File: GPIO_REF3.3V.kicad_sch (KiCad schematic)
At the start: 14 parts

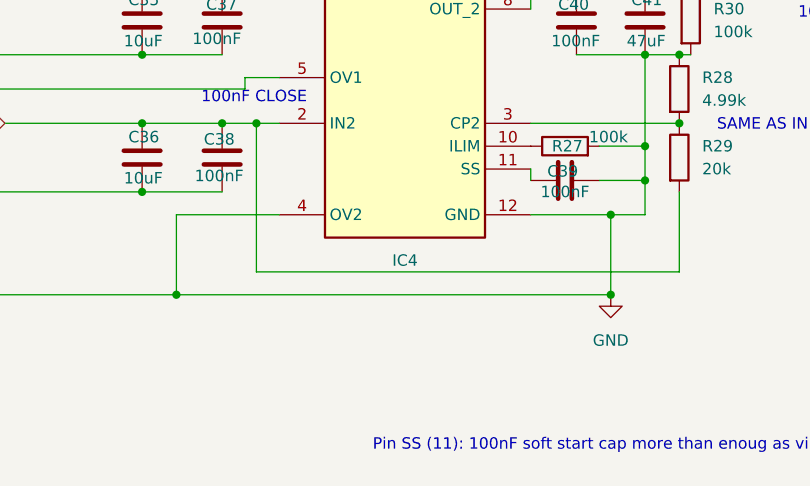
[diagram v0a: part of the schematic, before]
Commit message: added Gyroscope and Accelerometer part (4x) over IIC
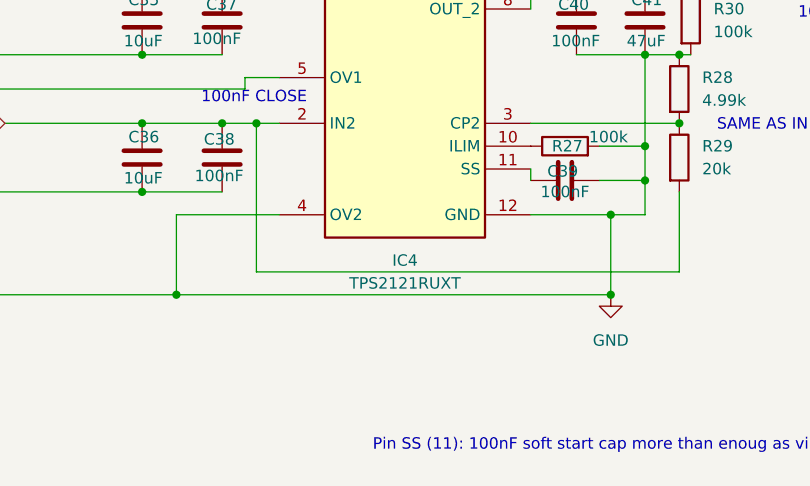
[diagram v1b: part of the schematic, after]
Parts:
- IC4: value ~ -> TPS2121RUXT
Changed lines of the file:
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@@
 			)
 		)
-		(property "Value" "~"
+		(property "Value" "TPS2121RUXT"
 			(at 146.05 121.92 0)
 			(effects

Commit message: multiple chainges on PCB
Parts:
- IC4: Order (none) -> Ordered=True
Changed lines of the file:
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@@
+			)
+		)
+		(property "Order" "Ordered=True"
+			(at 132.08 88.9 0)
+			(effects
+				(font
+					(size 1.27 1.27)
+				)
+				(hide yes)
 			)
 		)

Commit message: Power changes
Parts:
- renumbered IC4 to IC5, R14 to R25
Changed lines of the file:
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@@
 		)
 		(instances
-			(project ""
-				(path "/ce1819b2-f280-40ed-834f-6fe4d12f809d/c1998c4d-3f9a-4761-b447-a813532738a0/e46d3b44-477e-48ec-b385-9b4870813d66"
+			(project "nautilus_mainboard"
+				(path "/ce1819b2-f280-40ed-834f-6fe4d12f809d/c1998c4d-3f9a-4761-b447-a813532738a0/b9b676f4-45ad-4d4b-96a9-894c1f9d02cb"
 					(reference "C39")
 					(unit 1)
@@
 		(instances
 			(project "nautilus_mainboard"
-				(path "/ce1819b2-f280-40ed-834f-6fe4d12f809d/c1998c4d-3f9a-4761-b447-a813532738a0/e46d3b44-477e-48ec-b385-9b4870813d66"
+				(path "/ce1819b2-f280-40ed-834f-6fe4d12f809d/c1998c4d-3f9a-4761-b447-a813532738a0/b9b676f4-45ad-4d4b-96a9-894c1f9d02cb"
 					(reference "C40")
 					(unit 1)
@@
 		(instances
 			(project "nautilus_mainboard"
-				(path "/ce1819b2-f280-40ed-834f-6fe4d12f809d/c1998c4d-3f9a-4761-b447-a813532738a0/e46d3b44-477e-48ec-b385-9b4870813d66"
+				(path "/ce1819b2-f280-40ed-834f-6fe4d12f809d/c1998c4d-3f9a-4761-b447-a813532738a0/b9b676f4-45ad-4d4b-96a9-894c1f9d02cb"
 					(reference "R26")
 					(unit 1)
@@
 		(on_board yes)
 		(dnp no)
-		(property "Reference" "R14"
+		(property "Reference" "R25"
 			(at 129.54 87.122 90)
 			(effects
@@
 		(instances
 			(project "nautilus_mainboard"
-				(path "/ce1819b2-f280-40ed-834f-6fe4d12f809d/c1998c4d-3f9a-4761-b447-a813532738a0/e46d3b44-477e-48ec-b385-9b4870813d66"
-					(reference "R14")
+				(path "/ce1819b2-f280-40ed-834f-6fe4d12f809d/c1998c4d-3f9a-4761-b447-a813532738a0/b9b676f4-45ad-4d4b-96a9-894c1f9d02cb"
+					(reference "R25")
 					(unit 1)
 				)
@@
 		(instances
 			(project "nautilus_mainboard"
-				(path "/ce1819b2-f280-40ed-834f-6fe4d12f809d/c1998c4d-3f9a-4761-b447-a813532738a0/e46d3b44-477e-48ec-b385-9b4870813d66"
+				(path "/ce1819b2-f280-40ed-834f-6fe4d12f809d/c1998c4d-3f9a-4761-b447-a813532738a0/b9b676f4-45ad-4d4b-96a9-894c1f9d02cb"
 					(reference "R28")
 					(unit 1)
@@
 		(instances
 			(project "nautilus_mainboard"
-				(path "/ce1819b2-f280-40ed-834f-6fe4d12f809d/c1998c4d-3f9a-4761-b447-a813532738a0/e46d3b44-477e-48ec-b385-9b4870813d66"
+				(path "/ce1819b2-f280-40ed-834f-6fe4d12f809d/c1998c4d-3f9a-4761-b447-a813532738a0/b9b676f4-45ad-4d4b-96a9-894c1f9d02cb"
 					(reference "C37")
 					(unit 1)
@@
 		(dnp no)
 		(fields_autoplaced yes)
-		(property "Reference" "#PWR033"
+		(property "Reference" "#PWR030"
 			(at 168.91 129.54 0)
 			(effects
@@
 		(instances
 			(project "nautilus_mainboard"
-				(path "/ce1819b2-f280-40ed-834f-6fe4d12f809d/c1998c4d-3f9a-4761-b447-a813532738a0/e46d3b44-477e-48ec-b385-9b4870813d66"
-					(reference "#PWR033")
+				(path "/ce1819b2-f280-40ed-834f-6fe4d12f809d/c1998c4d-3f9a-4761-b447-a813532738a0/b9b676f4-45ad-4d4b-96a9-894c1f9d02cb"
+					(reference "#PWR030")
 					(unit 1)
 				)
@@
 		(instances
 			(project "nautilus_mainboard"
-				(path "/ce1819b2-f280-40ed-834f-6fe4d12f809d/c1998c4d-3f9a-4761-b447-a813532738a0/e46d3b44-477e-48ec-b385-9b4870813d66"
+				(path "/ce1819b2-f280-40ed-834f-6fe4d12f809d/c1998c4d-3f9a-4761-b447-a813532738a0/b9b676f4-45ad-4d4b-96a9-894c1f9d02cb"
 					(reference "C41")
 					(unit 1)
@@
 		(instances
 			(project "nautilus_mainboard"
-				(path "/ce1819b2-f280-40ed-834f-6fe4d12f809d/c1998c4d-3f9a-4761-b447-a813532738a0/e46d3b44-477e-48ec-b385-9b4870813d66"
+				(path "/ce1819b2-f280-40ed-834f-6fe4d12f809d/c1998c4d-3f9a-4761-b447-a813532738a0/b9b676f4-45ad-4d4b-96a9-894c1f9d02cb"
 					(reference "C35")
 					(unit 1)
@@
 		(instances
 			(project "nautilus_mainboard"
-				(path "/ce1819b2-f280-40ed-834f-6fe4d12f809d/c1998c4d-3f9a-4761-b447-a813532738a0/e46d3b44-477e-48ec-b385-9b4870813d66"
+				(path "/ce1819b2-f280-40ed-834f-6fe4d12f809d/c1998c4d-3f9a-4761-b447-a813532738a0/b9b676f4-45ad-4d4b-96a9-894c1f9d02cb"
 					(reference "R29")
 					(unit 1)
@@
 		)
 		(instances
-			(project ""
-				(path "/ce1819b2-f280-40ed-834f-6fe4d12f809d/c1998c4d-3f9a-4761-b447-a813532738a0/e46d3b44-477e-48ec-b385-9b4870813d66"
+			(project "nautilus_mainboard"
+				(path "/ce1819b2-f280-40ed-834f-6fe4d12f809d/c1998c4d-3f9a-4761-b447-a813532738a0/b9b676f4-45ad-4d4b-96a9-894c1f9d02cb"
 					(reference "R30")
 					(unit 1)
@@
 		(instances
 			(project "nautilus_mainboard"
-				(path "/ce1819b2-f280-40ed-834f-6fe4d12f809d/c1998c4d-3f9a-4761-b447-a813532738a0/e46d3b44-477e-48ec-b385-9b4870813d66"
+				(path "/ce1819b2-f280-40ed-834f-6fe4d12f809d/c1998c4d-3f9a-4761-b447-a813532738a0/b9b676f4-45ad-4d4b-96a9-894c1f9d02cb"
 					(reference "C38")
 					(unit 1)
@@
 		(instances
 			(project "nautilus_mainboard"
-				(path "/ce1819b2-f280-40ed-834f-6fe4d12f809d/c1998c4d-3f9a-4761-b447-a813532738a0/e46d3b44-477e-48ec-b385-9b4870813d66"
+				(path "/ce1819b2-f280-40ed-834f-6fe4d12f809d/c1998c4d-3f9a-4761-b447-a813532738a0/b9b676f4-45ad-4d4b-96a9-894c1f9d02cb"
 					(reference "R27")
 					(unit 1)
@@
 		(dnp no)
 		(fields_autoplaced yes)
-		(property "Reference" "IC4"
+		(property "Reference" "IC5"
 			(at 146.05 119.38 0)
 			(effects
@@
 		(instances
 			(project "nautilus_mainboard"
-				(path "/ce1819b2-f280-40ed-834f-6fe4d12f809d/c1998c4d-3f9a-4761-b447-a813532738a0/e46d3b44-477e-48ec-b385-9b4870813d66"
-					(reference "IC4")
+				(path "/ce1819b2-f280-40ed-834f-6fe4d12f809d/c1998c4d-3f9a-4761-b447-a813532738a0/b9b676f4-45ad-4d4b-96a9-894c1f9d02cb"
+					(reference "IC5")
 					(unit 1)
 				)
@@
 		(instances
 			(project "nautilus_mainboard"
-				(path "/ce1819b2-f280-40ed-834f-6fe4d12f809d/c1998c4d-3f9a-4761-b447-a813532738a0/e46d3b44-477e-48ec-b385-9b4870813d66"
+				(path "/ce1819b2-f280-40ed-834f-6fe4d12f809d/c1998c4d-3f9a-4761-b447-a813532738a0/b9b676f4-45ad-4d4b-96a9-894c1f9d02cb"
 					(reference "C36")
 					(unit 1)

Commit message: chore: more cleanup
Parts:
- removed C35, C36: 10uF, Capacitor_SMD:C_1210_3225Metric, symbol #dzdb:s_cap/C-MUR-GRM32EC72A106KE05
- removed C37, C38, C40: 100nF, Capacitor_SMD:C_0603_1608Metric, symbol #dzdb:g_cap/C-100n-0603
- removed C41: 47uF, Capacitor_SMD:C_0805_2012Metric, symbol #dzdb:s_cap/C-MUR-GRM21BR61A476ME15
- removed IC5: TPS2121RUXT, dz_dio:TI_Switchover_TPS2121RUXT, symbol #dzdb:s_misc/TEXA-595-TPS2121RUXT
- removed R25: 15.4k, Resistor_SMD:R_0603_1608Metric, symbol #dzdb:g_res/R-15.4k-0603
- removed R26, R28: 4.99k, Resistor_SMD:R_0603_1608Metric, symbol #dzdb:g_res/R-4.99k-0603
- removed R29: 20k, Resistor_SMD:R_0603_1608Metric, symbol #dzdb:g_res/R-20k-0603
- removed R30: 100k, Resistor_SMD:R_0603_1608Metric, symbol #dzdb:g_res/R-100k-0603
- added C48, C49: 10uF, Capacitor_SMD:C_1210_3225Metric, symbol #dzdb:s_cap/C-MUR-GRM32EC72A106KE05
- added C50, C51, C52: 100nF, Capacitor_SMD:C_0603_1608Metric, symbol #dzdb:g_cap/C-100n-0603
- added C54: 47uF, Capacitor_SMD:C_0805_2012Metric, symbol #dzdb:s_cap/C-MUR-GRM21BR61A476ME15
- added IC3: TPS2121RUXT, dz_dio:TI_Switchover_TPS2121RUXT, symbol #dzdb:s_misc/TEXA-595-TPS2121RUXT
- added R14: 100k, Resistor_SMD:R_0603_1608Metric, symbol #dzdb:g_res/R-100k-0603
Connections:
- net CM4_OUT_3.3V: now also C49.1, C51.1, IC3.2 (IN2)
- net GND: now also C39.1, R27.1, C48.2, C49.2, C50.2, C51.2, C52.2, C54.2, IC3.12 (GND), IC3.3 (CP2), IC3.4 (OV2), IC3.5 (OV1), R14.2; no longer C39.2, R27.2
- net GPIO_VREF_3.3V: now also C52.1, C54.1, IC3.1 (OUT_1), IC3.8 (OUT_2), R14.1
- net STM_IN_3.3V: now also C48.1, C50.1, IC3.6 (PR1), IC3.7 (IN1)
- new net: C39.2, IC3.11 (SS)
- new net: IC3.10 (ILIM), R27.2
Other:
- note removed: "100nF CLOSE"
- note removed: "SAME AS IN 5V"
- note removed: "V-div (same ratio as 5V)"
- company: (none) -> Davide
- moved on the sheet: C39, R27

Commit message: chore: Loads of redoing stuff. Added a Changelog
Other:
- title: (none) -> Nautilus_Mainboard
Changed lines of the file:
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@@
 	(paper "A4")
 	(title_block
+		(title "Nautilus_Mainboard")
 		(date "2025-11-19")
 		(rev "0")

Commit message: chore: routed many parts together. added testpoints
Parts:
- added TP13: Test Point, TestPoint:TestPoint_Pad_D1.5mm, symbol #dzdb:g_mech/M-TEST-SMT_1.5mm_round
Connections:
- net GPIO_VREF_3.3V: now also TP13.1
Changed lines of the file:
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@@
+		)
+	)
+	(symbol
+		(lib_id "#dzdb:g_mech/M-TEST-SMT_1.5mm_round")
+		(at 172.72 77.47 0)
+		(unit 1)
+		(exclude_from_sim no)
+		(in_bom yes)
+		(on_board yes)
+		(dnp no)
+		(property "Reference" "TP13"
+			(at 175.26 72.8979 0)
+			(effects
+				(font
+					(size 1.27 1.27)
+				)
+				(justify left)
+			)
+		)
+		(property "Value" "Test Point"
+			(at 175.26 74.93 0)
+			(effects
+				(font
+					(size 1.27 1.27)
+				)
+				(justify left)
+			)
+		)
+		(property "Footprint" "TestPoint:TestPoint_Pad_D1.5mm"
+			(at 177.8 77.47 0)
+			(effects
+				(font
+					(size 1.27 1.27)
+				)
+				(hide yes)
+			)
+		)
+		(property "Datasheet" "~"
+			(at 177.8 77.47 0)
+			(effects
+				(font
+					(size 1.27 1.27)
+				)
+				(hide yes)
+			)
+		)
+		(property "Description" "SMT Test Point 1.5mm round"
+			(at 172.72 77.47 0)
+			(effects
+				(font
+					(size 1.27 1.27)
+				)
+				(hide yes)
+			)
+		)
+		(property "IPN" "M-TEST-SMT_1.5mm_round"
+			(at 172.72 77.47 0)
+			(effects
+				(font
+					(size 1.27 1.27)
+				)
+				(hide yes)
+			)
+		)
+		(property "Comments" "TestPoint 1.5mm"
+			(at 172.72 77.47 0)
+			(effects
+				(font
+					(size 1.27 1.27)
+				)
+				(hide yes)
+			)
+		)
+		(pin "1"
+		)
+		(instances
+			(project "nautilus_mainboard"
+				(path "/ce1819b2-f280-40ed-834f-6fe4d12f809d/c1998c4d-3f9a-4761-b447-a813532738a0/b9b676f4-45ad-4d4b-96a9-894c1f9d02cb"
+					(reference "TP13")
+					(unit 1)
+				)
+			)
 		)
 	)
